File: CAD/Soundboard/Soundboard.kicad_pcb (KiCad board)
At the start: 2 copper layers, 105 x 85 mm, 53 parts, among them J1 USB-C, Q1 IRLML6401, Q2 IRLML6401, Q3 IRLML6401, Q4 IRLML6401, SW1 SW_SPST, SW10 SW_SPST, SW11 SW_SPST, SW12 SW_SPST, SW13 SW_SPST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

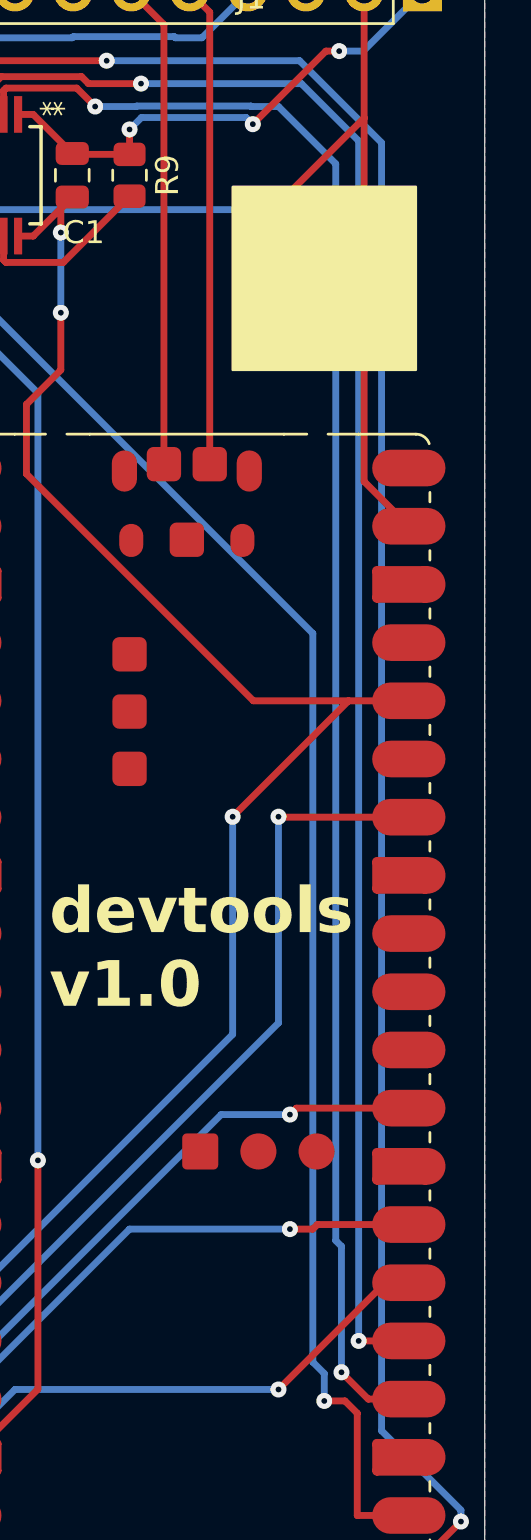
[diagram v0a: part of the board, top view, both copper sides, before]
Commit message: swap led sclk and sin
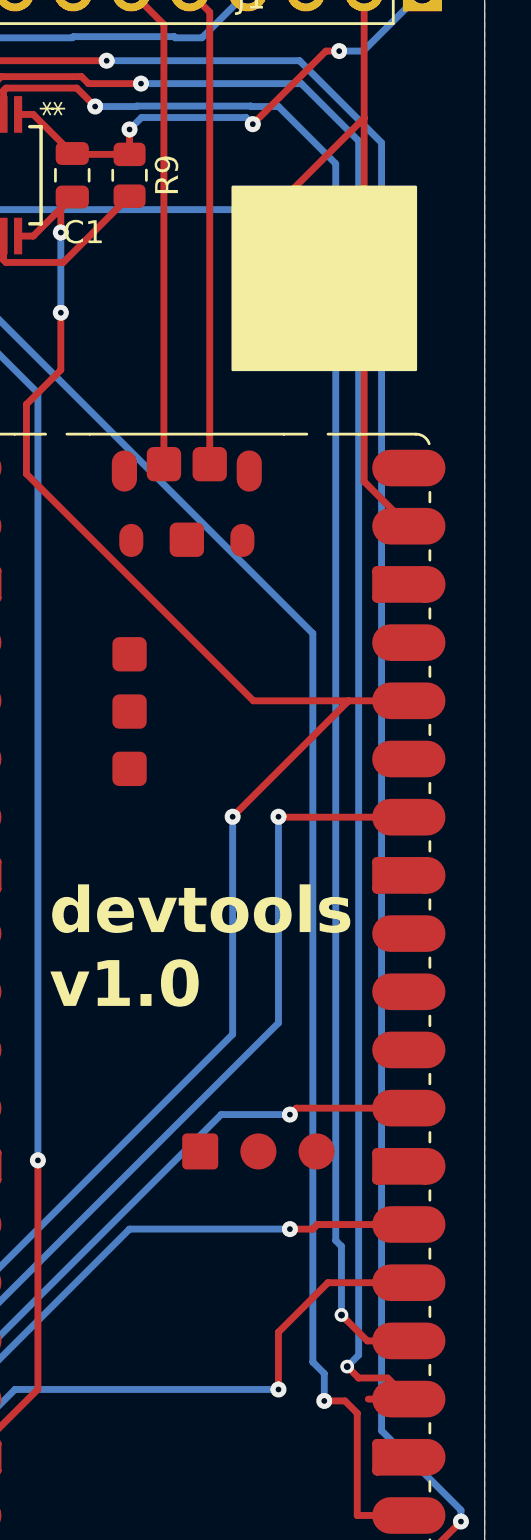
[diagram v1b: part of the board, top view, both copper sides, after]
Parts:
- J1: value USB-C -> USB4085-GF-A_REVB
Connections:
- A1 pad 24: /LED SIN -> /LED SCLK
- A1 pad 25: /LED SCLK -> /LED SIN
- A1 pad 37: +3.3V -> unconnected-(A1-3V3_EN-Pad37)
- C1 pad 2: /3V3 -> Net-(U1-VCC)
- Q1 pad 2: /VBUS -> Net-(Q1-S)
- Q2 pad 2: /VBUS -> Net-(Q1-S)
- Q3 pad 2: /VBUS -> Net-(Q1-S)
- Q4 pad 2: /VBUS -> Net-(Q1-S)
- R5 pad 1: /VBUS -> Net-(Q1-S)
- R6 pad 1: /VBUS -> Net-(Q1-S)
- R7 pad 1: /VBUS -> Net-(Q1-S)
- R8 pad 1: /VBUS -> Net-(Q1-S)
- U1 pad 24: /3V3 -> Net-(U1-VCC)
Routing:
- net /LED SCLK: track 73.3 -> 77.4 mm
- net /LED SIN: track 73.3 -> 71.1 mm
- net /SCREEN_SDA: track 89.9 -> 91.4 mm

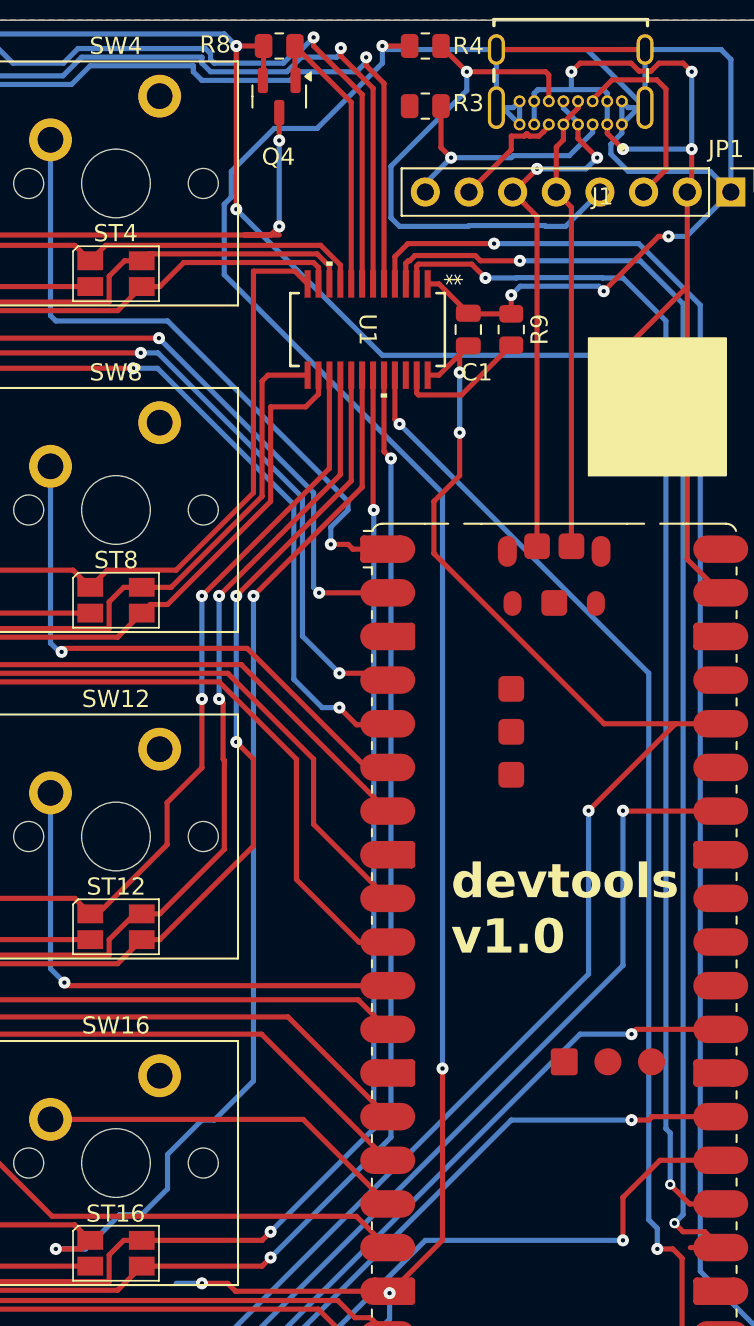
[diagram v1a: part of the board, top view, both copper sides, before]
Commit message: move some caps
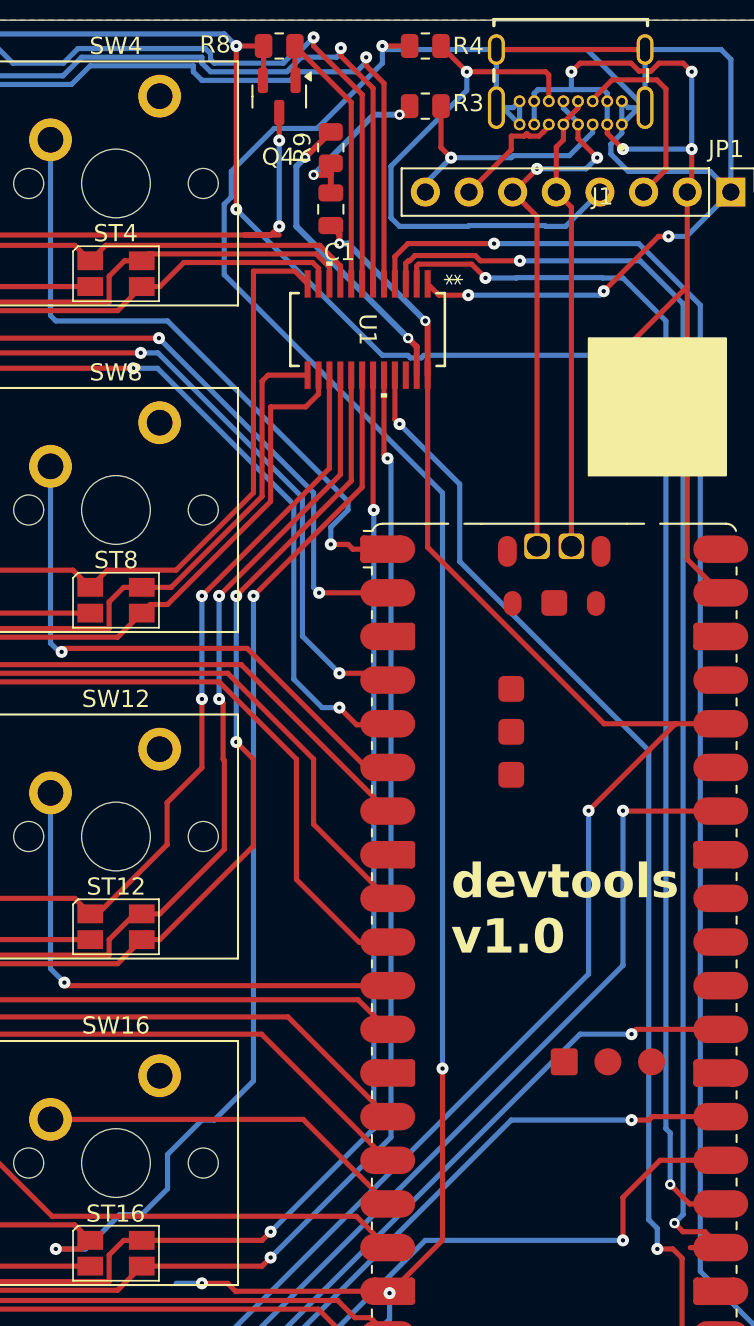
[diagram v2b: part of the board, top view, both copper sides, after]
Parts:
- moved R9 14.9 mm to (107.5, 35.9), turned to 90 degrees
- moved C1 10.6 mm to (107.5, 39.5)
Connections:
- C1 pad 2: Net-(U1-VCC) -> /3V3
- U1 pad 24: Net-(U1-VCC) -> /3V3
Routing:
- net Net-(U1-IREF): track 7.79 -> 17.9 mm, vias 0 -> 2
- net GND: track 263.9 -> 272.0 mm, vias 9 -> 11
- net /3V3: track 145.2 -> 151.1 mm
